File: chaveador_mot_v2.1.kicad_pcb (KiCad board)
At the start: 2 copper layers, 43.5 x 37 mm, 12 parts, among them J1 Screw_Terminal_01x02, J2 Screw_Terminal_01x02, Q1 IRF9540N, U1 4N25

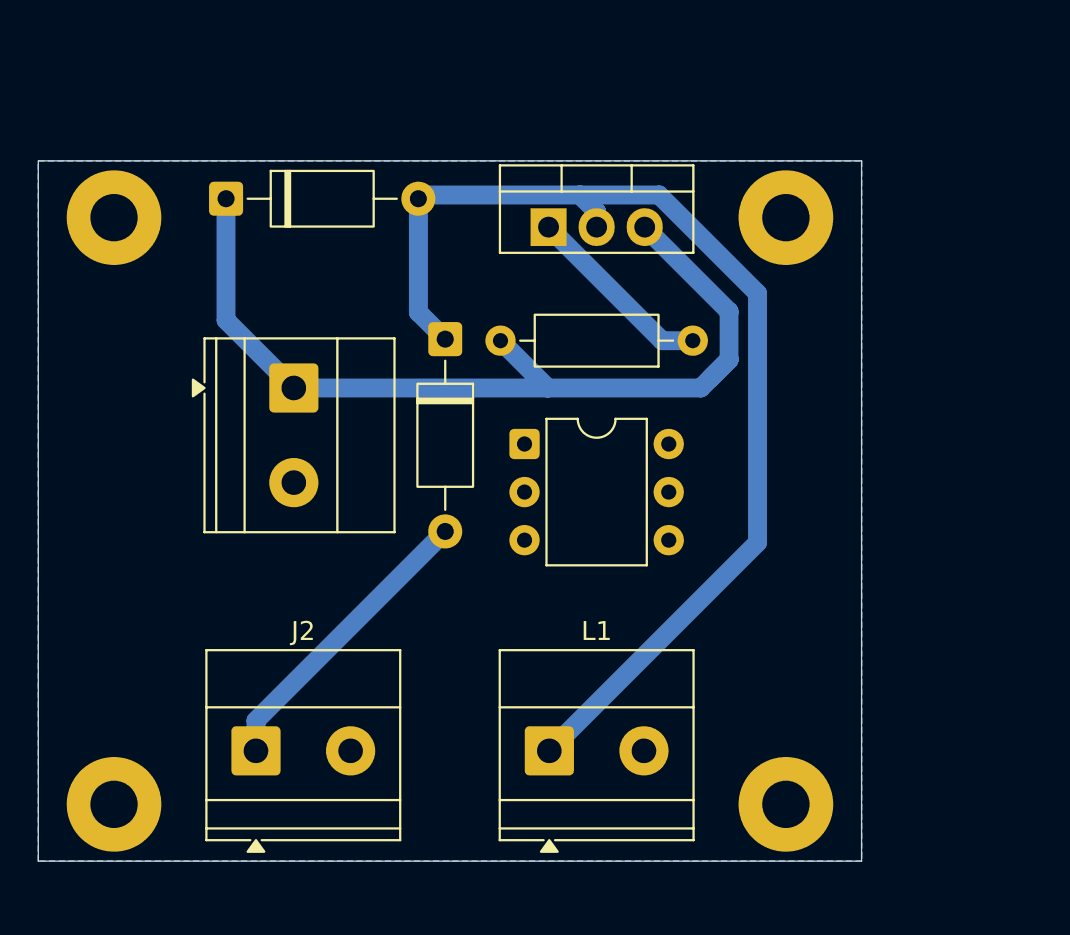
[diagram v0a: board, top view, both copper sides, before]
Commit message: coloquei a entrada do sinal para o un425 e rearranjei a pcb para conctar tudo
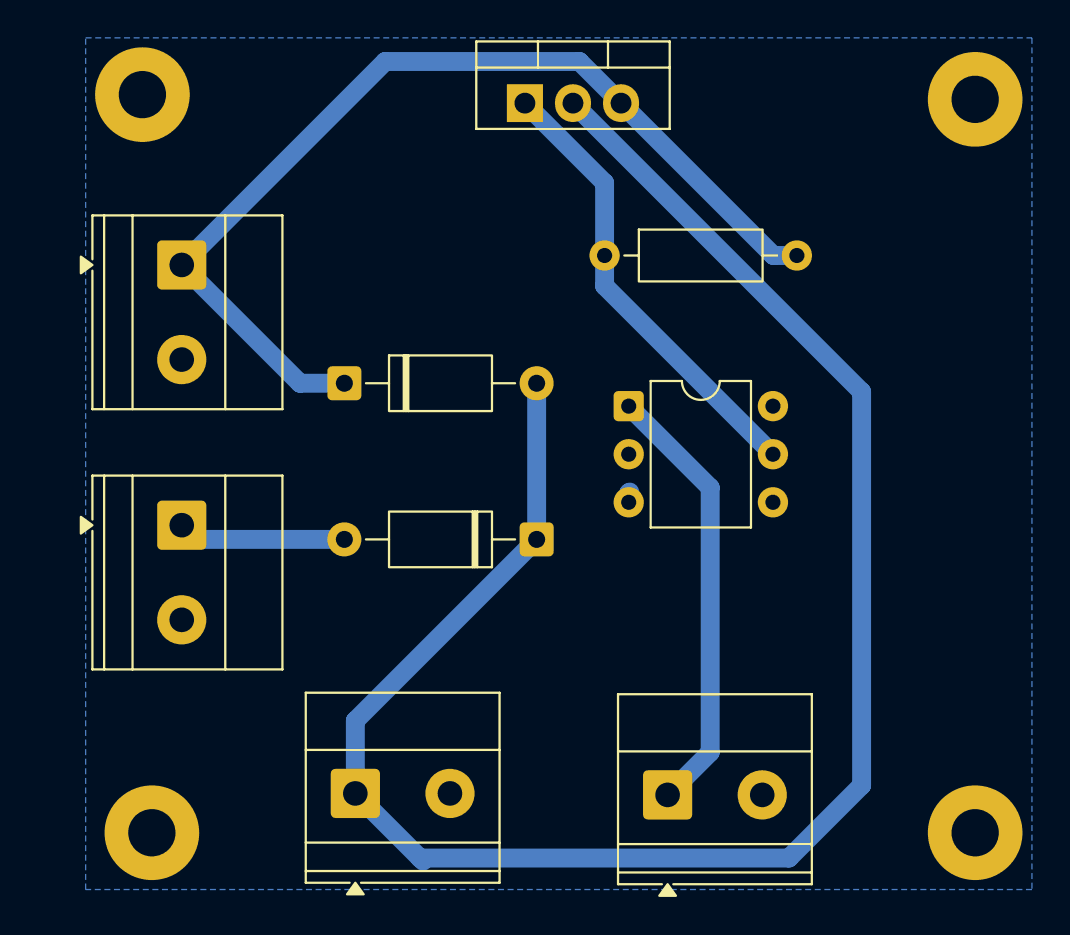
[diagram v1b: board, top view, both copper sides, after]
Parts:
- added J3: Screw_Terminal_01x02, TerminalBlock_Phoenix:TerminalBlock_Phoenix_MKDS-1,5-2_1x02_P5.00mm_Horizontal, F.Cu at (55.8, 65.0)
- moved J2 12.6 mm to (30.1, 50.8), turned to -90 degrees
- moved H1 11.8 mm to (72.0, 28.2)
- moved D2 11.6 mm to (48.8, 51.5), turned to 180 degrees
- moved D1 11.6 mm to (38.7, 43.2)
- moved L1 10.5 mm to (39.2, 64.9)
- moved H4 10.1 mm to (72.0, 67.0)
- moved J1 8.79 mm to (30.1, 37.0)
- moved H2 6.67 mm to (28.0, 28.0)
- moved Q1 6.67 mm to (48.2, 28.4)
- moved R1 6.48 mm to (52.4, 36.5), turned to 0 degrees
- moved U1 5.86 mm to (53.7, 44.5)
- moved H3 2.50 mm to (28.5, 67.0)
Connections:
- U1 pad 1: unconnected-(U1-Pad1) -> Sinal
- U1 pad 2: unconnected-(U1-Pad2) -> GND
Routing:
- net Net-(D1-A): track 59.0 -> 98.0 mm
- net Sinal: track 0.00 -> 23.3 mm
- net Net-(Q1-G): track 10.1 -> 24.0 mm
- net Vcn24: track 15.7 -> 8.90 mm
- net Vcc: track 48.9 -> 52.1 mm
- removed copper zone on B.Cu, net (none)
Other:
- board outline removed
